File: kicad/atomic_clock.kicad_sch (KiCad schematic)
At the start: 78 parts, among them J1 Conn_02x05_Top_Bottom, J10 Conn_02x05_Top_Bottom, J11 Conn_02x05_Top_Bottom, J12 USB_B_Micro, J13 Conn_ARM_JTAG_SWD_10, J14 Conn_01x03_Female, J2 Conn_02x05_Top_Bottom, J3 Conn_02x05_Top_Bottom, J4 Conn_02x05_Top_Bottom, J5 USB_B_Micro, J6 Conn_02x05_Top_Bottom, J7 Conn_02x05_Top_Bottom, J8 Conn_02x05_Top_Bottom, J9 Conn_02x05_Top_Bottom, Q1 Q_Dual_PMOS, Q2 Q_Dual_PMOS, SW1 SW_Push, U1 D198K, U10 ATSAMDA1E16B-A, U11 D198K, U12 D198K, U13 D198K, U14 D198K, U15 D198K, U16 MAX7221xWG, U17 D198K, U18 D198K, U19 D198K, U2 D198K, U20 NCP1117LPST33T3G, U21 mems_osc_st1630, U22 DHT20, U23 DCF77, U24 MCP73831-2-OT, U25 TXB0101, U3 D198K, U4 D198K, U5 MAX7221xWG, U6 D198K, U7 D198K, U8 D198K, U9 D198K

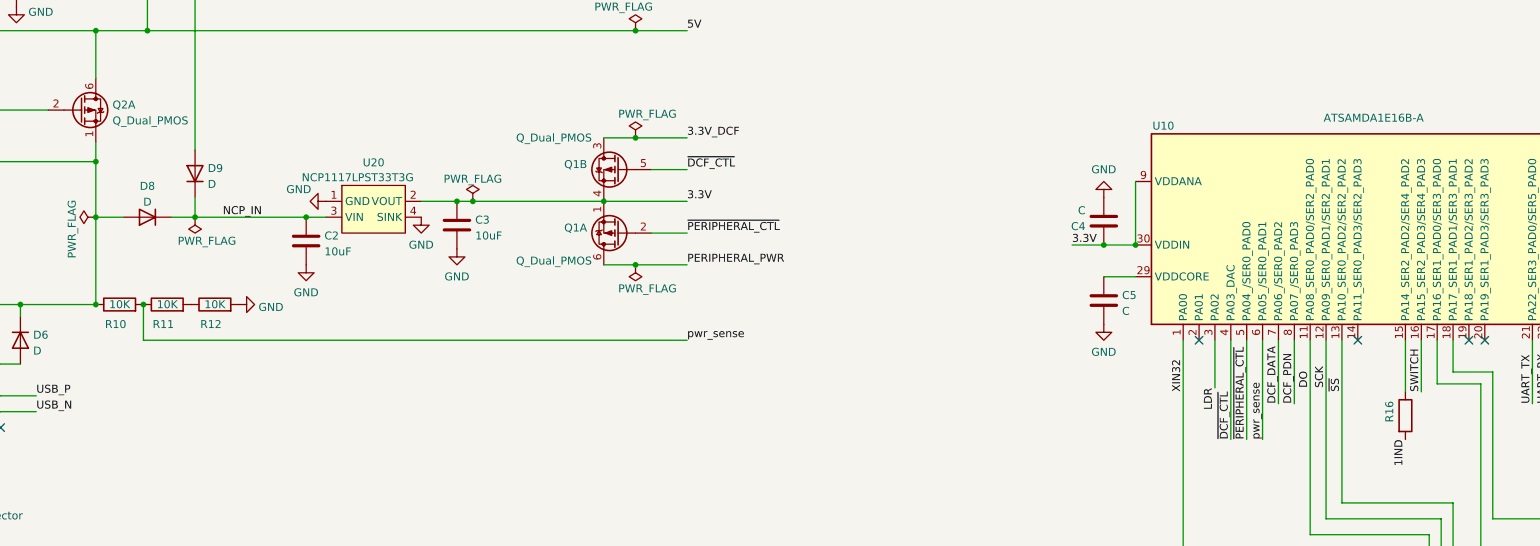
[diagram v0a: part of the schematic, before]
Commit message: Switch Pfet from NTJD4152P to si1965dh due to availability
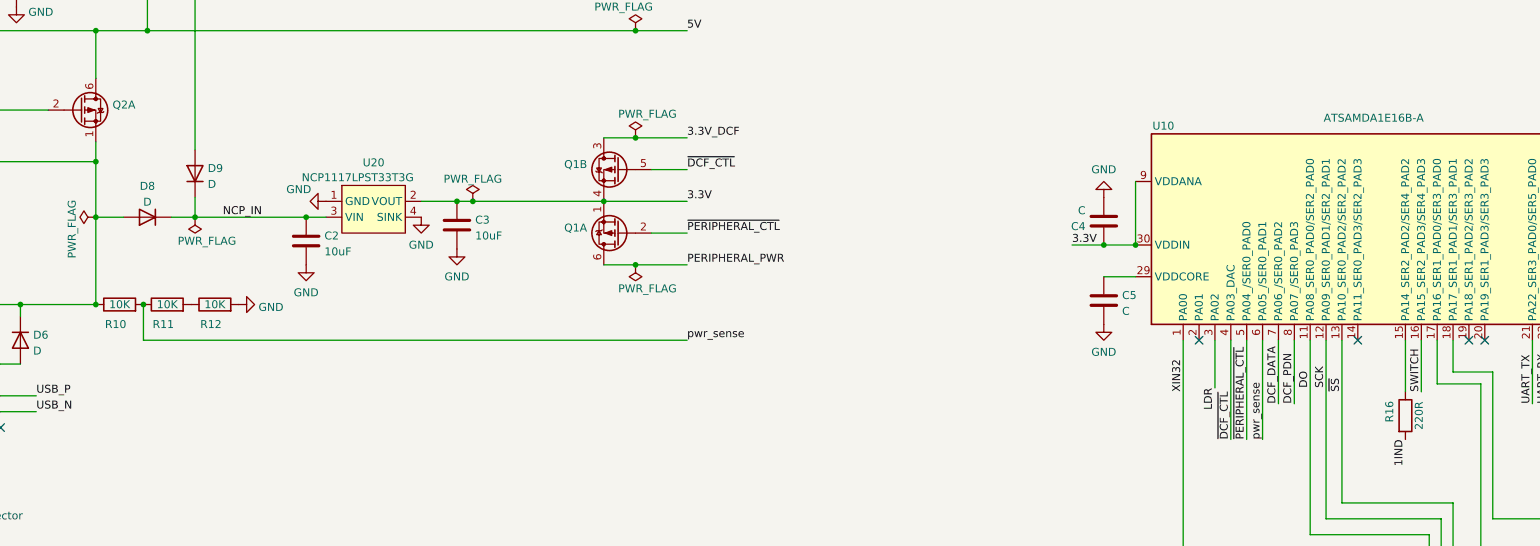
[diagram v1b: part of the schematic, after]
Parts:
- Q1, Q2: value Q_Dual_PMOS -> (none); footprint Package_TO_SOT_SMD:SOT-363_SC-70-6 -> (none); Mfr No. (none) -> SI1965DH-T1-BE3
- R16: value (none) -> 220R; footprint (none) -> Resistor_SMD:R_0805_2012Metric
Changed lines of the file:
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@@
       (effects (font (size 1.27 1.27)) (justify left))
     )
-    (property "Value" "Q_Dual_PMOS" (id 1) (at 102.362 86.1572 0)
-      (effects (font (size 1.27 1.27)) (justify left))
-    )
-    (property "Footprint" "Package_TO_SOT_SMD:SOT-363_SC-70-6" (id 2) (at 98.425 84.455 0)
-      (effects (font (size 1.27 1.27)) hide)
-    )
-    (property "Datasheet" "~" (id 3) (at 98.425 84.455 0)
+    (property "Value" "" (id 1) (at 102.362 86.1572 0)
+      (effects (font (size 1.27 1.27)) (justify left))
+    )
+    (property "Footprint" "" (id 2) (at 98.425 84.455 0)
+      (effects (font (size 1.27 1.27)) hide)
+    )
+    (property "Datasheet" "https://www.mouser.be/datasheet/2/427/si1965dh-1764856.pdf" (id 3) (at 98.425 84.455 0)
+      (effects (font (size 1.27 1.27)) hide)
+    )
+    (property "Mfr No." " SI1965DH-T1-BE3 " (id 4) (at 97.155 84.455 0)
       (effects (font (size 1.27 1.27)) hide)
     )
@@
     (in_bom yes) (on_board yes)
     (property "Reference" "R16" (id 0) (at 306.705 132.715 90))
-    (property "Value" "" (id 1) (at 311.4239 133.35 90))
-    (property "Footprint" "" (id 2) (at 307.467 133.35 90)
+    (property "Value" "220R" (id 1) (at 311.4239 133.35 90))
+    (property "Footprint" "Resistor_SMD:R_0805_2012Metric" (id 2) (at 307.467 133.35 90)
       (effects (font (size 1.27 1.27)) hide)
     )
@@
       (effects (font (size 1.27 1.27)) (justify left))
     )
-    (property "Value" "Q_Dual_PMOS" (id 1) (at 179.07 108.585 0)
-      (effects (font (size 1.27 1.27)) (justify left))
-    )
-    (property "Footprint" "Package_TO_SOT_SMD:SOT-363_SC-70-6" (id 2) (at 182.245 104.14 0)
-      (effects (font (size 1.27 1.27)) hide)
-    )
-    (property "Datasheet" "https://www.mouser.be/datasheet/2/308/NTJD4152P_D-115296.pdf" (id 3) (at 182.245 104.14 0)
+    (property "Value" "" (id 1) (at 179.07 108.585 0)
+      (effects (font (size 1.27 1.27)) (justify left))
+    )
+    (property "Footprint" "" (id 2) (at 182.245 104.14 0)
+      (effects (font (size 1.27 1.27)) hide)
+    )
+    (property "Datasheet" "https://www.mouser.be/datasheet/2/427/si1965dh-1764856.pdf" (id 3) (at 182.245 104.14 0)
+      (effects (font (size 1.27 1.27)) hide)
+    )
+    (property "Mfr No." " SI1965DH-T1-BE3" (id 4) (at 183.515 104.14 0)
       (effects (font (size 1.27 1.27)) hide)
     )
@@
       (effects (font (size 1.27 1.27)) (justify left))
     )
-    (property "Value" "Q_Dual_PMOS" (id 1) (at 179.07 88.9 0)
-      (effects (font (size 1.27 1.27)) (justify left))
-    )
-    (property "Footprint" "Package_TO_SOT_SMD:SOT-363_SC-70-6" (id 2) (at 182.245 93.98 0)
-      (effects (font (size 1.27 1.27)) hide)
-    )
-    (property "Datasheet" "https://www.mouser.be/datasheet/2/308/NTJD4152P_D-115296.pdf" (id 3) (at 182.245 93.98 0)
-      (effects (font (size 1.27 1.27)) hide)
-    )
+    (property "Value" "" (id 1) (at 179.07 88.9 0)
+      (effects (font (size 1.27 1.27)) (justify left))
+    )
+    (property "Footprint" "" (id 2) (at 182.245 93.98 0)
+      (effects (font (size 1.27 1.27)) hide)
+    )
+    (property "Datasheet" "https://www.mouser.be/datasheet/2/427/si1965dh-1764856.pdf" (id 3) (at 182.245 93.98 0)
+      (effects (font (size 1.27 1.27)) hide)
+    )
+    (property "Mfr No." " SI1965DH-T1-BE3" (id 4) (at 183.515 104.14 0)
+      (effects (font (size 1.27 1.27)) hide)
+    )

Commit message: Switched flat top LEDs
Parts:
- D1, D2, D3, D4: value LED -> (none); footprint LED_THT:LED_D3.0mm_FlatTop -> (none)
- Q1, Q2: value (none) -> Q_Dual_PMOS; footprint (none) -> Package_TO_SOT_SMD:SOT-363_SC-70-6
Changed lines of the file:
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@@
       (effects (font (size 1.27 1.27)) (justify left))
     )
-    (property "Value" "" (id 1) (at 102.362 86.1572 0)
-      (effects (font (size 1.27 1.27)) (justify left))
-    )
-    (property "Footprint" "" (id 2) (at 98.425 84.455 0)
+    (property "Value" "Q_Dual_PMOS" (id 1) (at 102.362 86.1572 0)
+      (effects (font (size 1.27 1.27)) (justify left))
+    )
+    (property "Footprint" "Package_TO_SOT_SMD:SOT-363_SC-70-6" (id 2) (at 98.425 84.455 0)
       (effects (font (size 1.27 1.27)) hide)
     )
@@
       (effects (font (size 1.27 1.27)) (justify left))
     )
-    (property "Value" "" (id 1) (at 179.07 108.585 0)
-      (effects (font (size 1.27 1.27)) (justify left))
-    )
-    (property "Footprint" "" (id 2) (at 182.245 104.14 0)
+    (property "Value" "Q_Dual_PMOS" (id 1) (at 179.07 108.585 0)
+      (effects (font (size 1.27 1.27)) (justify left))
+    )
+    (property "Footprint" "Package_TO_SOT_SMD:SOT-363_SC-70-6" (id 2) (at 182.245 104.14 0)
       (effects (font (size 1.27 1.27)) hide)
     )
@@
     (in_bom yes) (on_board yes) (fields_autoplaced)
     (property "Reference" "D3" (id 0) (at 465.1375 292.5912 0))
-    (property "Value" "LED" (id 1) (at 465.1375 295.1281 0))
-    (property "Footprint" "LED_THT:LED_D3.0mm_FlatTop" (id 2) (at 463.55 298.45 0)
-      (effects (font (size 1.27 1.27)) hide)
-    )
-    (property "Datasheet" "~" (id 3) (at 463.55 298.45 0)
+    (property "Value" "" (id 1) (at 465.1375 295.1281 0))
+    (property "Footprint" "" (id 2) (at 463.55 298.45 0)
+      (effects (font (size 1.27 1.27)) hide)
+    )
+    (property "Datasheet" "https://www.mouser.be/datasheet/2/239/lite-on_lites03148-1-1737336.pdf" (id 3) (at 463.55 298.45 0)
       (effects (font (size 1.27 1.27)) hide)
     )
@@
       (effects (font (size 1.27 1.27)) (justify left))
     )
-    (property "Value" "" (id 1) (at 179.07 88.9 0)
-      (effects (font (size 1.27 1.27)) (justify left))
-    )
-    (property "Footprint" "" (id 2) (at 182.245 93.98 0)
+    (property "Value" "Q_Dual_PMOS" (id 1) (at 179.07 88.9 0)
+      (effects (font (size 1.27 1.27)) (justify left))
+    )
+    (property "Footprint" "Package_TO_SOT_SMD:SOT-363_SC-70-6" (id 2) (at 182.245 93.98 0)
       (effects (font (size 1.27 1.27)) hide)
     )
@@
     (in_bom yes) (on_board yes) (fields_autoplaced)
     (property "Reference" "D1" (id 0) (at 390.2075 292.5912 0))
-    (property "Value" "LED" (id 1) (at 390.2075 295.1281 0))
-    (property "Footprint" "LED_THT:LED_D3.0mm_FlatTop" (id 2) (at 388.62 298.45 0)
-      (effects (font (size 1.27 1.27)) hide)
-    )
-    (property "Datasheet" "~" (id 3) (at 388.62 298.45 0)
+    (property "Value" "" (id 1) (at 390.2075 295.1281 0))
+    (property "Footprint" "" (id 2) (at 388.62 298.45 0)
+      (effects (font (size 1.27 1.27)) hide)
+    )
+    (property "Datasheet" "https://www.mouser.be/datasheet/2/239/lite-on_lites03148-1-1737336.pdf" (id 3) (at 388.62 298.45 0)
       (effects (font (size 1.27 1.27)) hide)
     )
@@
     (in_bom yes) (on_board yes)
     (property "Reference" "D4" (id 0) (at 463.2325 298.9412 0))
-    (property "Value" "LED" (id 1) (at 465.1375 301.4781 0))
-    (property "Footprint" "LED_THT:LED_D3.0mm_FlatTop" (id 2) (at 463.55 304.8 0)
-      (effects (font (size 1.27 1.27)) hide)
-    )
-    (property "Datasheet" "~" (id 3) (at 463.55 304.8 0)
+    (property "Value" "" (id 1) (at 465.1375 301.4781 0))
+    (property "Footprint" "" (id 2) (at 463.55 304.8 0)
+      (effects (font (size 1.27 1.27)) hide)
+    )
+    (property "Datasheet" "https://www.mouser.be/datasheet/2/239/lite-on_lites03148-1-1737336.pdf" (id 3) (at 463.55 304.8 0)
       (effects (font (size 1.27 1.27)) hide)
     )
@@
     (in_bom yes) (on_board yes)
     (property "Reference" "D2" (id 0) (at 388.3025 298.9412 0))
-    (property "Value" "LED" (id 1) (at 390.2075 301.4781 0))
-    (property "Footprint" "LED_THT:LED_D3.0mm_FlatTop" (id 2) (at 388.62 304.8 0)
-      (effects (font (size 1.27 1.27)) hide)
-    )
-    (property "Datasheet" "~" (id 3) (at 388.62 304.8 0)
+    (property "Value" "" (id 1) (at 390.2075 301.4781 0))
+    (property "Footprint" "" (id 2) (at 388.62 304.8 0)
+      (effects (font (size 1.27 1.27)) hide)
+    )
+    (property "Datasheet" "https://www.mouser.be/datasheet/2/239/lite-on_lites03148-1-1737336.pdf" (id 3) (at 388.62 304.8 0)
       (effects (font (size 1.27 1.27)) hide)
     )
@@
     )
     (path "/40e4542f-fd07-4d9d-9833-4cdfd4ae69d2"
-      (reference "D1") (unit 1) (value "LED") (footprint "LED_THT:LED_D3.0mm_FlatTop")
+      (reference "D1") (unit 1) (value "LED") (footprint "local_footprints:LED_D2.0mm_W4.8mm_H2.5mm_FlatTop")
     )
     (path "/effe650d-9aad-4b3f-a47b-82b3588d185f"
-      (reference "D2") (unit 1) (value "LED") (footprint "LED_THT:LED_D3.0mm_FlatTop")
+      (reference "D2") (unit 1) (value "LED") (footprint "local_footprints:LED_D2.0mm_W4.8mm_H2.5mm_FlatTop")
     )
     (path "/349f3b48-8efc-4b54-a997-e0f0f4797c8d"
-      (reference "D3") (unit 1) (value "LED") (footprint "LED_THT:LED_D3.0mm_FlatTop")
+      (reference "D3") (unit 1) (value "LED") (footprint "local_footprints:LED_D2.0mm_W4.8mm_H2.5mm_FlatTop")
     )
     (path "/b2e1e60c-b210-4f6a-b120-5e652e54aed6"
-      (reference "D4") (unit 1) (value "LED") (footprint "LED_THT:LED_D3.0mm_FlatTop")
+      (reference "D4") (unit 1) (value "LED") (footprint "local_footprints:LED_D2.0mm_W4.8mm_H2.5mm_FlatTop")
     )
     (path "/9ad349d5-a248-4ca5-aef5-ebd538d72f9a"

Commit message: Filled out datasheet and part numbers on almost all components
So we can generate a BOM.
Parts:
- added C11: 10uF CL21A106KPFNNNF, Capacitor_SMD:C_0805_2012Metric, symbol Device:C
- BT1: value Battery_Cell -> (none); footprint local_footprints:Battery_pads -> (none)
- C1, C6, C7, C8: value 100nF -> (none); footprint Capacitor_SMD:C_0805_2012Metric -> (none)
- C10, C9: value 4.7uF -> (none); footprint Capacitor_SMD:C_0805_2012Metric -> (none)
- C2, C3: value 10uF -> (none); footprint Capacitor_SMD:C_0805_2012Metric -> (none)
- C4, C5: value C -> (none); footprint Capacitor_SMD:C_0805_2012Metric -> (none)
- D5, D6, D8, D9: value D -> (none); footprint Diode_SMD:D_SMA -> (none)
- D7: value LED -> (none); footprint LED_SMD:LED_1206_3216Metric_Pad1.42x1.75mm_HandSolder -> (none)
- J12: value USB_B_Micro -> (none); footprint Connector_USB:USB_Micro-B_Amphenol_10118194_Horizontal -> (none)
- J13: value Conn_ARM_JTAG_SWD_10 -> (none); footprint local_footprints:sam_swd_header -> (none); Notes (none) -> http://infocenter.arm.com/help/topic/com.arm.doc.ddi0314h/D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
- J5: value USB_B_Micro -> (none); footprint Connector_USB:USB_Micro-B_Molex-105133-0001 -> (none)
- R1, R10, R11, R12, R13, R14, R15, R3, R4, R5, R7, R9: value 10K -> (none); footprint Resistor_SMD:R_0805_2012Metric -> (none)
- R2: value 1K -> (none); footprint Resistor_SMD:R_0805_2012Metric -> (none); Mfr (none) -> RC0805FR-101KL
- R6: value R_Photo -> (none); footprint OptoDevice:R_LDR_4.9x4.2mm_P2.54mm_Vertical -> (none)
- R8: value 330R -> (none); footprint Resistor_SMD:R_0805_2012Metric -> (none); Mfr (none) -> RK73H2ATTD4700F
- SW1: value SW_Push -> (none); footprint Button_Switch_SMD:SW_SPST_TL3342 -> (none); Mfr (none) -> TL3342F160QG
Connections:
- net 3.3V: now also C11.1
- net GND: now also C11.2

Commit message: Added general indicator LED
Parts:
- added D10: LED HSMS-C150, LED_SMD:LED_1206_3216Metric_Pad1.42x1.75mm_HandSolder, symbol Device:LED
- BT1: value (none) -> Varta CP1654 A3; footprint (none) -> local_footprints:Battery_pads
- C1, C4, C6, C7, C8: value (none) -> 100nF 885012207016; footprint (none) -> Capacitor_SMD:C_0805_2012Metric
- C10, C9: value (none) -> 4.7uF CL21A475KPFNNNE; footprint (none) -> Capacitor_SMD:C_0805_2012Metric
- C2, C3: value (none) -> 10uF CL21A106KPFNNNF; footprint (none) -> Capacitor_SMD:C_0805_2012Metric
- C5: value (none) -> 1uF 885012207051; footprint (none) -> Capacitor_SMD:C_0805_2012Metric
- D1, D2, D3, D4: value (none) -> LED LTL-1224A; footprint (none) -> local_footprints:LED_D2.0mm_W4.8mm_H2.5mm_FlatTop
- D5, D6, D8, D9: value (none) -> Diode S1M-13-F; footprint (none) -> Diode_SMD:D_SMA
- D7: value (none) -> LED HSMS-C150; footprint (none) -> LED_SMD:LED_1206_3216Metric_Pad1.42x1.75mm_HandSolder
- J12: value (none) -> USB_B_Micro 10118194-0001LF; footprint (none) -> Connector_USB:USB_Micro-B_Amphenol_10118194_Horizontal
- J13: value (none) -> ARM_JTAG_SWD_10 3220-10-0100-00; footprint (none) -> local_footprints:sam_swd_header
- J5: value (none) -> USB_B_Micro 1051330001; footprint (none) -> Connector_USB:USB_Micro-B_Molex-105133-0001
- R1, R10, R11, R12, R13, R14, R15, R3, R4, R5, R7, R9: value (none) -> 10K; footprint (none) -> Resistor_SMD:R_0805_2012Metric
- R2: value (none) -> 1K; footprint (none) -> Resistor_SMD:R_0805_2012Metric
- R6: value (none) -> LDR NSL-19M51; footprint (none) -> OptoDevice:R_LDR_4.9x4.2mm_P2.54mm_Vertical
- R8: value (none) -> 470R; footprint (none) -> Resistor_SMD:R_0805_2012Metric
- SW1: value (none) -> SW_Push; footprint (none) -> Button_Switch_SMD:SW_SPST_TL3342
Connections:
- net 3DP2: now also U19.5 (DP)
- net GND: now also D10.1 (K)
- net at R16.1: now also D10.2 (A); no longer U10.15 (PA14_SER2_PAD2/SER4_PAD2)
- net 1IND: no longer names the net of J10.7 (Pin_7)
- net 1IND: no longer R16.2
- net 3IND: no longer names the net of J11.7 (Pin_7)
- net 3IND: no longer U19.5 (DP)
- new net INDICATOR: R16.2, U10.15 (PA14_SER2_PAD2/SER4_PAD2)
- no-connect marks 35 -> 37
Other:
- note added: "Front facing general indicator LED"
- moved on the sheet: R16

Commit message: Getting ready for v1.0
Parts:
- U3: value D198K -> (none); footprint Display_7Segment:D1X8K -> (none)
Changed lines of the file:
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@@
     (in_bom yes) (on_board yes) (fields_autoplaced)
     (property "Reference" "U3" (id 0) (at 138.43 288.4002 0))
-    (property "Value" "D198K" (id 1) (at 138.43 290.9371 0))
-    (property "Footprint" "Display_7Segment:D1X8K" (id 2) (at 138.43 320.04 0)
+    (property "Value" "" (id 1) (at 138.43 290.9371 0))
+    (property "Footprint" "" (id 2) (at 138.43 320.04 0)
       (effects (font (size 1.27 1.27)) hide)
     )

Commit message: Version 1.0 for submission to JLCPCB
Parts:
- U3: value (none) -> D198K; footprint (none) -> Display_7Segment:D1X8K
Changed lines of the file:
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@@
     (in_bom yes) (on_board yes) (fields_autoplaced)
     (property "Reference" "U3" (id 0) (at 138.43 288.4002 0))
-    (property "Value" "" (id 1) (at 138.43 290.9371 0))
-    (property "Footprint" "" (id 2) (at 138.43 320.04 0)
+    (property "Value" "D198K" (id 1) (at 138.43 290.9371 0))
+    (property "Footprint" "Display_7Segment:D1X8K" (id 2) (at 138.43 320.04 0)
       (effects (font (size 1.27 1.27)) hide)
     )

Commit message: Add appr prices to BOM
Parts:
- BT1: value Varta CP1654 A3 -> (none); footprint local_footprints:Battery_pads -> (none); Notes (none) -> https://www.aliexpress.com/item/1005002477897458.html; Price (none) -> 6.14
- C1, C4, C6, C7, C8: value 100nF 885012207016 -> (none); footprint Capacitor_SMD:C_0805_2012Metric -> (none); Price (none) -> 0.045
- C10, C9: value 4.7uF CL21A475KPFNNNE -> (none); footprint Capacitor_SMD:C_0805_2012Metric -> (none); Price (none) -> 0.041
- C11, C2, C3: value 10uF CL21A106KPFNNNF -> (none); footprint Capacitor_SMD:C_0805_2012Metric -> (none); Price (none) -> 0.072
- C5: value 1uF 885012207051 -> (none); footprint Capacitor_SMD:C_0805_2012Metric -> (none); Price (none) -> 0.08
- D1, D2, D3, D4: value LED LTL-1224A -> (none); footprint local_footprints:LED_D2.0mm_W4.8mm_H2.5mm_FlatTop -> (none); Mfr No. (none) -> LTL-1224A; Mouser (none) -> https://www.mouser.be/ProductDetail/859-LTL-1224A; Price (none) -> 0.253
- D10, D7: value LED HSMS-C150 -> (none); footprint LED_SMD:LED_1206_3216Metric_Pad1.42x1.75mm_HandSolder -> (none); Price (none) -> 0.252
- D5, D6, D8, D9: value Diode S1M-13-F -> (none); footprint Diode_SMD:D_SMA -> (none); Price (none) -> 0.213
- J1, J10, J11, J2, J3, J4, J6, J7, J8, J9: value Conn_02x05_Top_Bottom -> (none); footprint Connector_PinHeader_2.54mm:PinHeader_2x05_P2.54mm_Vertical -> (none); DigiKey (none) -> 67996-400HLF; Price (none) -> 0.2416
- J12: value USB_B_Micro 10118194-0001LF -> (none); footprint Connector_USB:USB_Micro-B_Amphenol_10118194_Horizontal -> (none); DigiKey (none) -> https://www.digikey.lu/en/products/detail/amphenol-cs-fci/1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; Price (none) -> 0.48
- J13: value ARM_JTAG_SWD_10 3220-10-0100-00 -> (none); footprint local_footprints:sam_swd_header -> (none); DigiKey (none) -> https://www.digikey.lu/en/products/detail/cnc-tech/3220-10-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; Price (none) -> 0.557
- J14: value Conn_01x03_Female -> (none); footprint Connector_PinSocket_2.54mm:PinSocket_1x03_P2.54mm_Vertical -> (none); DigiKey (none) -> https://www.digikey.lu/en/products/detail/adam-tech/SMC-1-0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; Price (none) -> 0.27
- J5: value USB_B_Micro 1051330001 -> (none); footprint Connector_USB:USB_Micro-B_Molex-105133-0001 -> (none); DigiKey (none) -> https://www.digikey.lu/en/products/detail/molex/1051330001/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; Price (none) -> 1.17
- Q1: value Q_Dual_PMOS -> (none); footprint Package_TO_SOT_SMD:SOT-363_SC-70-6 -> (none); Price (none) -> 0.431
- Q2: value Q_Dual_PMOS -> (none); footprint Package_TO_SOT_SMD:SOT-363_SC-70-6 -> (none); Mfr No. SI1965DH-T1-BE3 -> SI1965DH-T1-BE3; Price (none) -> 0.431
- R1, R10, R11, R12, R13, R14, R15, R3, R4, R5, R7, R9: value 10K -> (none); footprint Resistor_SMD:R_0805_2012Metric -> (none); Price (none) -> 0.017
- R16: value 220R -> (none); footprint Resistor_SMD:R_0805_2012Metric -> (none); Mfr (none) -> SG73S2ATTD2200F; Mouser (none) -> https://www.mouser.be/ProductDetail/KOA-Speer/SG73S2ATTD220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; Price (none) -> 0.161
- R2: value 1K -> (none); footprint Resistor_SMD:R_0805_2012Metric -> (none); Price (none) -> 0.029
- R6: value LDR NSL-19M51 -> (none); footprint OptoDevice:R_LDR_4.9x4.2mm_P2.54mm_Vertical -> (none); Price (none) -> 1.628
- R8: value 470R -> (none); footprint Resistor_SMD:R_0805_2012Metric -> (none); Price (none) -> 0.042
- SW1: value SW_Push -> (none); footprint Button_Switch_SMD:SW_SPST_TL3342 -> (none); Price (none) -> 0.58
- U1, U11, U12, U13, U14, U15, U17, U18, U19, U2, U3, U4, U6, U7, U8, U9: value D198K -> (none); footprint Display_7Segment:D1X8K -> (none)
- U10: value ATSAMDA1E16B-A -> (none); footprint Package_QFP:TQFP-32_7x7mm_P0.8mm -> (none); Price (none) -> 4.51
- U16, U5: value MAX7221xWG -> (none); footprint Package_SO:SOIC-24W_7.5x15.4mm_P1.27mm -> (none); Price (none) -> 10.77
- U20: value NCP1117LPST33T3G -> (none); footprint Package_TO_SOT_SMD:SOT-223 -> (none); Price (none) -> 0.437
- U21: value mems_osc_st1630 -> (none); footprint Package_TO_SOT_SMD:SOT-23-5 -> (none); Price (none) -> 2.45
- U22: value DHT20 -> (none); footprint local_footprints:DHT20 -> (none); Price (none) -> 6.18
- U23: value DCF77 -> (none); footprint local_footprints:DCF77 receiver module -> (none); Notes (none) -> https://www.amazon.nl/gp/product/B014I7VUS6/ref=ppx_yo_dt_b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; Price (none) -> 14.48
- U24: value MCP73831-2-OT -> (none); footprint Package_TO_SOT_SMD:SOT-23-5 -> (none); Price (none) -> 0.726
- U25: value TXB0101 -> (none); footprint Package_TO_SOT_SMD:SOT-363_SC-70-6 -> (none); Price (none) -> 0.509
